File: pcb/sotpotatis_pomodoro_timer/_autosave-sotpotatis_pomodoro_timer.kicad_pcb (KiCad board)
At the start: 4 copper layers, 81.1 x 58.7 mm, 57 parts, among them J2 USB_C_PWR_IN, SW1 LEFT_BTN, SW2 PRESET_1_BTN, SW3 PRESET_2_BTN, SW4 PRESET_3_BTN, SW5 RIGHT_BTN, SW6 PWR_SWITCH, U1 ATtiny84A-P

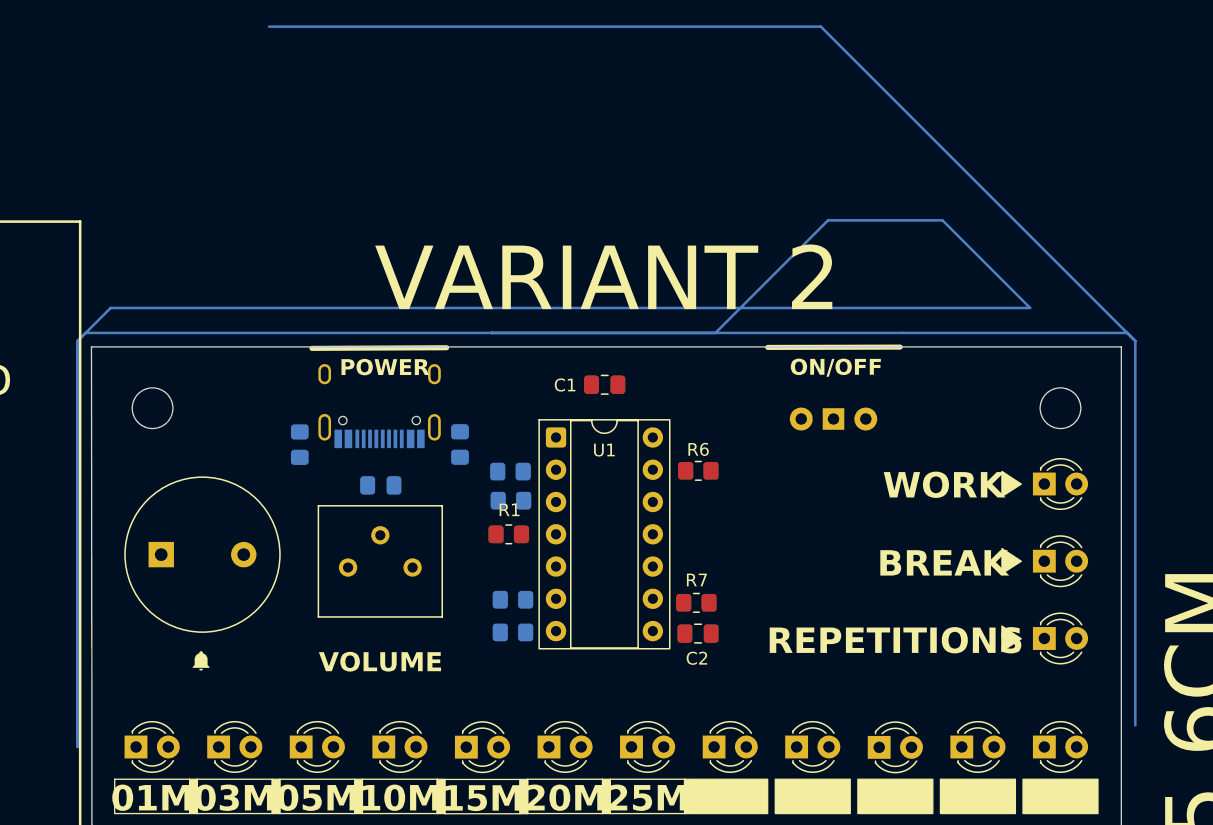
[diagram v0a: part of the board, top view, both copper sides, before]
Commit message: fix: Remove 1M shield resistor, component relabels for better layout
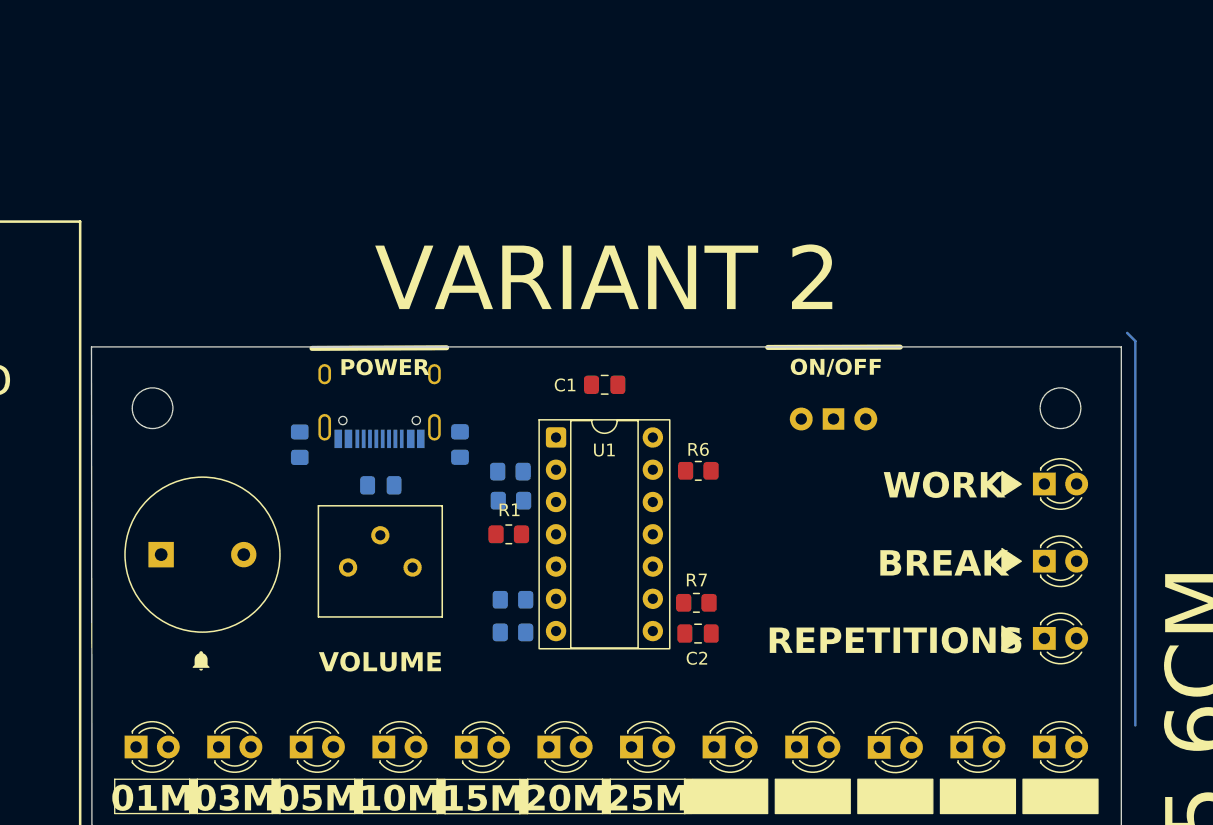
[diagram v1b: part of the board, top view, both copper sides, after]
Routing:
- net (no net): track 381.5 -> 31.2 mm
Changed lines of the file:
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@@
-	)
-	(segment
-		(start 155.341 41.854)
-		(end 91.064648 41.854)
-		(width 0.2)
-		(layer "B.Cu")
-		(net 0)
-	)
-	(segment
-		(start 90.452971 74.450937)
-		(end 90.419 74.416966)
-		(width 0.2)
-		(layer "B.Cu")
-		(net 0)
-	)
-	(segment
-		(start 91.064648 41.854)
-		(end 90.419492 42.499156)
-		(width 0.2)
-		(layer "B.Cu")
-		(net 0)
-	)
-	(segment
-		(start 140.647 41.854)
-		(end 123.008 41.854)
-		(width 0.2)
-		(layer "B.Cu")
-		(net 0)
-	)
-	(segment
-		(start 90.419492 43.411541)
-		(end 90.452508 74.021373)
-		(width 0.2)
-		(layer "B.Cu")
-		(net 0)
-	)
-	(segment
-		(start 158.511 32.992)
-		(end 149.509 32.992)
-		(width 0.2)
-		(layer "B.Cu")
-		(net 0)
-	)
-	(segment
-		(start 105.503 17.746)
-		(end 148.938049 17.746)
-		(width 0.2)
-		(layer "B.Cu")
-		(net 0)
 	)
 	(segment
@@
 	)
 	(segment
-		(start 90.419 74.416966)
-		(end 90.419 42.498951)
-		(width 0.2)
-		(layer "B.Cu")
-		(net 0)
-	)
-	(segment
 		(start 173.691 42.498951)
 		(end 173.691 72.745)
 		(width 0.2)
 		(layer "B.Cu")
-		(net 0)
-	)
-	(segment
-		(start 90.452508 74.021373)
-		(end 90.452971 74.450937)
-		(width 0.2)
-		(layer "B.Cu")
-		(net 0)
-	)
-	(segment
-		(start 165.409 39.89)
-		(end 158.511 32.992)
-		(width 0.2)
-		(layer "B.Cu")
-		(net 0)
-	)
-	(segment
-		(start 148.938049 17.746)
-		(end 173.691 42.498951)
-		(width 0.2)
-		(layer "B.Cu")
-		(net 0)
-	)
-	(segment
-		(start 93.027951 39.89)
-		(end 165.409 39.89)
-		(width 0.2)
-		(layer "B.Cu")
-		(net 0)
-	)
-	(segment
-		(start 123.008 41.854)
-		(end 123.08 41.854)
-		(width 0.2)
-		(layer "B.Cu")
-		(net 0)
-	)
-	(segment
-		(start 149.509 32.992)
-		(end 140.647 41.854)
-		(width 0.2)
-		(layer "B.Cu")
-		(net 0)
-	)
-	(segment
-		(start 90.419492 42.499156)
-		(end 90.419492 43.411541)
-		(width 0.2)
-		(layer "B.Cu")
-		(net 0)
-	)
-	(segment
-		(start 90.419 42.498951)
-		(end 93.027951 39.89)
-		(width 0.2)
-		(layer "B.Cu")
-		(net 0)
-	)
-	(segment
-		(start 173.046049 41.854)
-		(end 155.341 41.854)
-		(width 0.2)
-		(layer "B.Cu")
